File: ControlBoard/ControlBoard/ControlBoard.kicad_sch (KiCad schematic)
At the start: 30 parts, among them J10 PWR_IN, J12 FITPC, J13 SENS, J14 VBAT, J16 5V, J17 FAN, J2 Port, J3 USB_B_Mini, J4 PRT, J5 Stb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

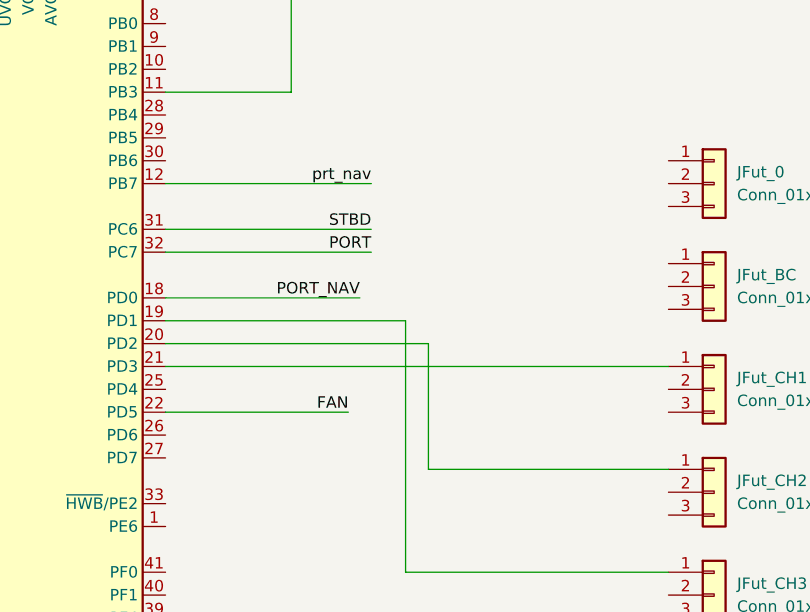
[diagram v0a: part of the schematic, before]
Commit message: Controller board compiling, no real code yet.
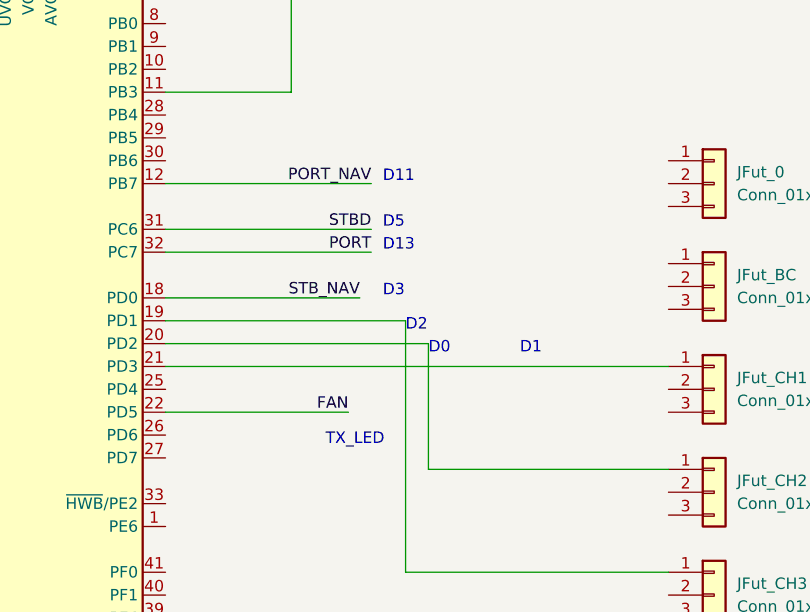
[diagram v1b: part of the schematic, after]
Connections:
- net prt_nav is gone; now on net PORT_NAV: U?.12 (PB7)
- net PORT_NAV: no longer U?.18 (PD0)
- new net STB_NAV: U?.18 (PD0)
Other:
- note added: "D0"
- note added: "D1"
- note added: "D11"
- note added: "D13"
- note added: "D2"
- note added: "D3"
- note added: "D5"
- note added: "TX_LED"
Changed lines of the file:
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@@
     (stroke (width 0) (type default) (color 0 0 0 0))
+  )
+  (text "TX_LED" (at 106.68 99.06 0)
+    (effects (font (size 1.27 1.27)) (justify left bottom))
+  )
+  (text "D1" (at 128.27 88.9 0)
+    (effects (font (size 1.27 1.27)) (justify left bottom))
+  )
+  (text "D11" (at 113.03 69.85 0)
+    (effects (font (size 1.27 1.27)) (justify left bottom))
+  )
+  (text "D5" (at 113.03 74.93 0)
+    (effects (font (size 1.27 1.27)) (justify left bottom))
+  )
+  (text "D13" (at 113.03 77.47 0)
+    (effects (font (size 1.27 1.27)) (justify left bottom))
+  )
+  (text "D3" (at 113.03 82.55 0)
+    (effects (font (size 1.27 1.27)) (justify left bottom))
+  )
+  (text "D2" (at 115.57 86.36 0)
+    (effects (font (size 1.27 1.27)) (justify left bottom))
+  )
+  (text "D0" (at 118.11 88.9 0)
+    (effects (font (size 1.27 1.27)) (justify left bottom))
   )
   (label "MOSI" (at 140.97 44.45 180)
@@
     (effects (font (size 1.27 1.27)) (justify right bottom))
   )
-  (label "PORT_NAV" (at 110.49 82.55 180)
+  (label "STB_NAV" (at 110.49 82.55 180)
     (effects (font (size 1.27 1.27)) (justify right bottom))
   )
@@
     (effects (font (size 1.27 1.27)) (justify left bottom))
   )
-  (label "prt_nav" (at 111.76 69.85 180)
+  (label "PORT_NAV" (at 111.76 69.85 180)
     (effects (font (size 1.27 1.27)) (justify right bottom))
   )

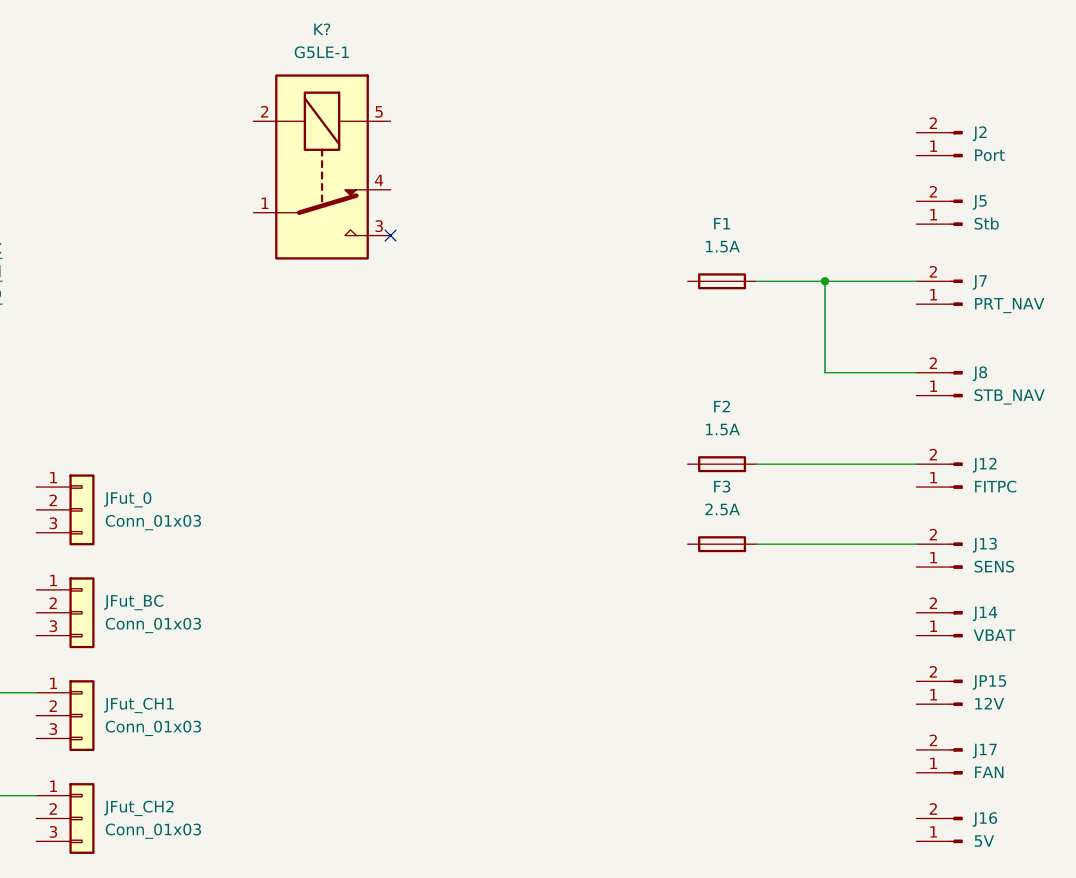
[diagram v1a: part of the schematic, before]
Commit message: added more board details as I discover them and backups and instructions for the existing uC code.
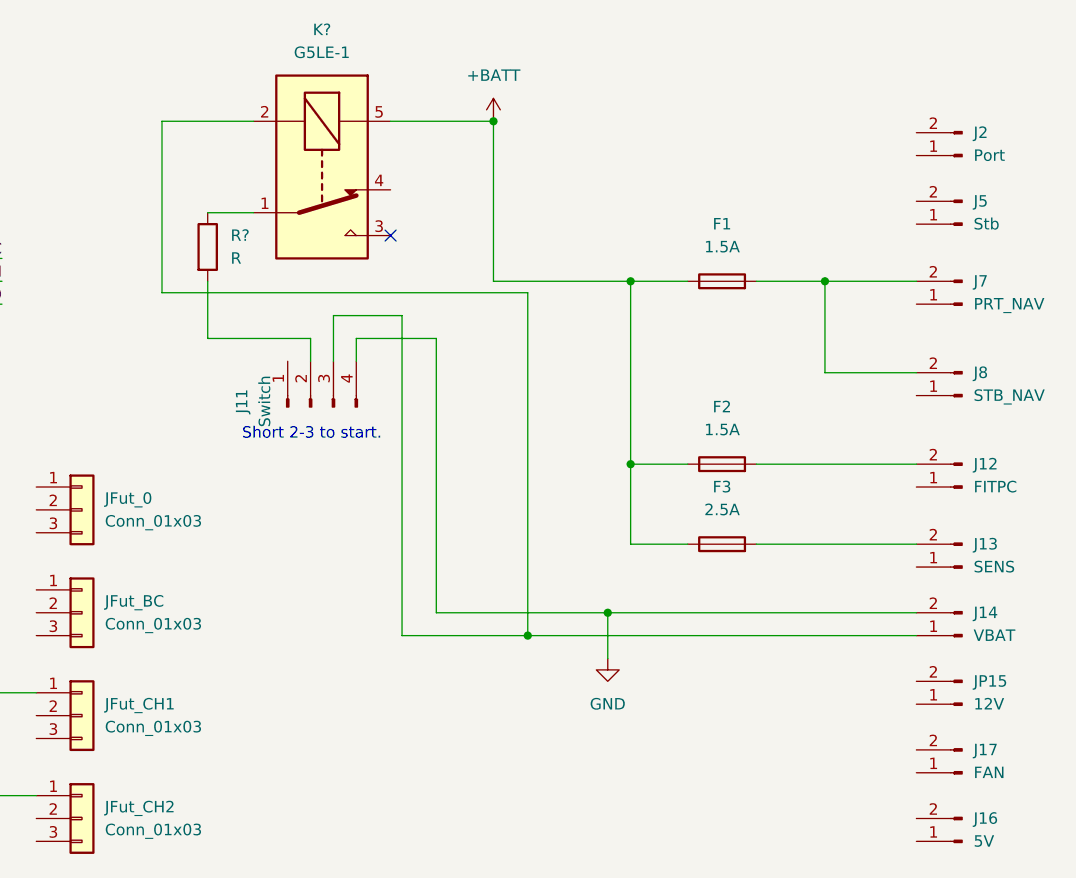
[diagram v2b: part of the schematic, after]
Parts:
- added J11: Switch, symbol Connector:Conn_01x04_Male
- added R?: R, symbol Device:R
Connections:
- net +BATT: now also F1.1, F2.1, F3.1, K?.5
- net GND: now also J14.2 (Pin_2), J11.4 (Pin_4)
- net at K?.1: now also R?.1
- net at K?.2: now also J14.1 (Pin_1), J11.3 (Pin_3)
- new net: J11.2 (Pin_2), R?.2
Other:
- note added: "Short 2-3 to start."

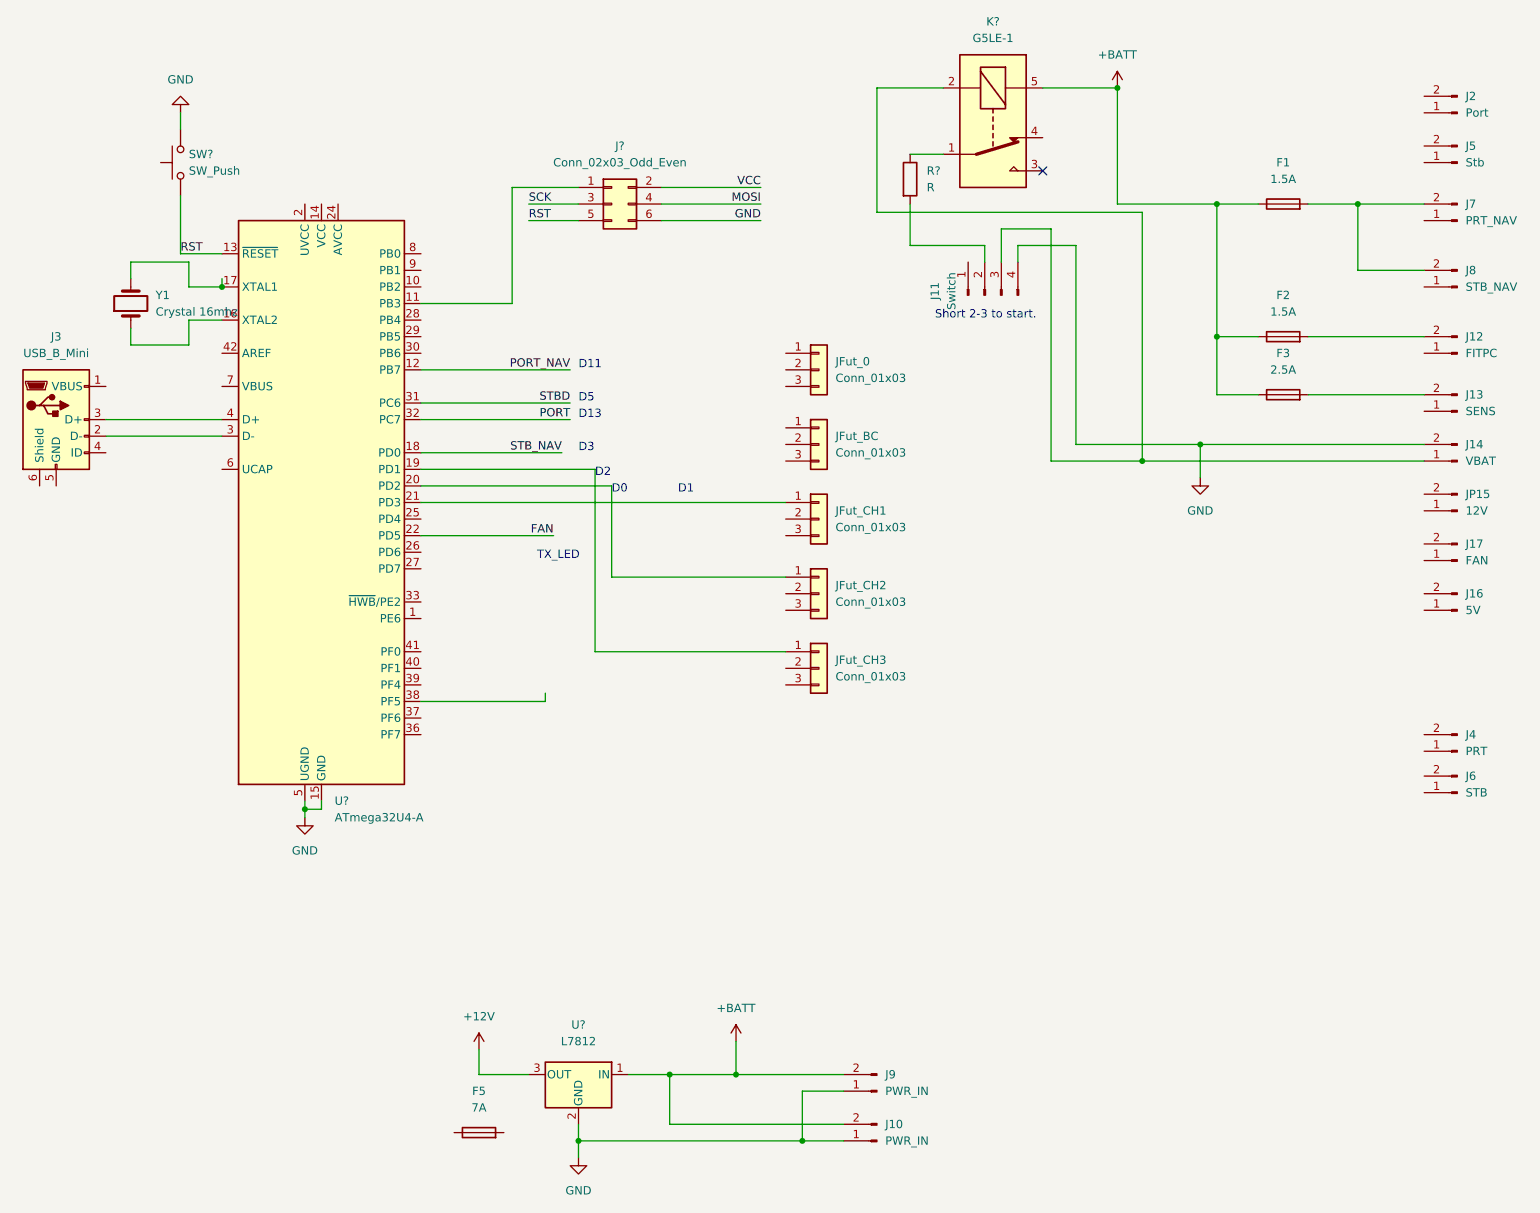
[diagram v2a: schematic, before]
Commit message: updated backup script instructions, updated control board diagram and pinouts.
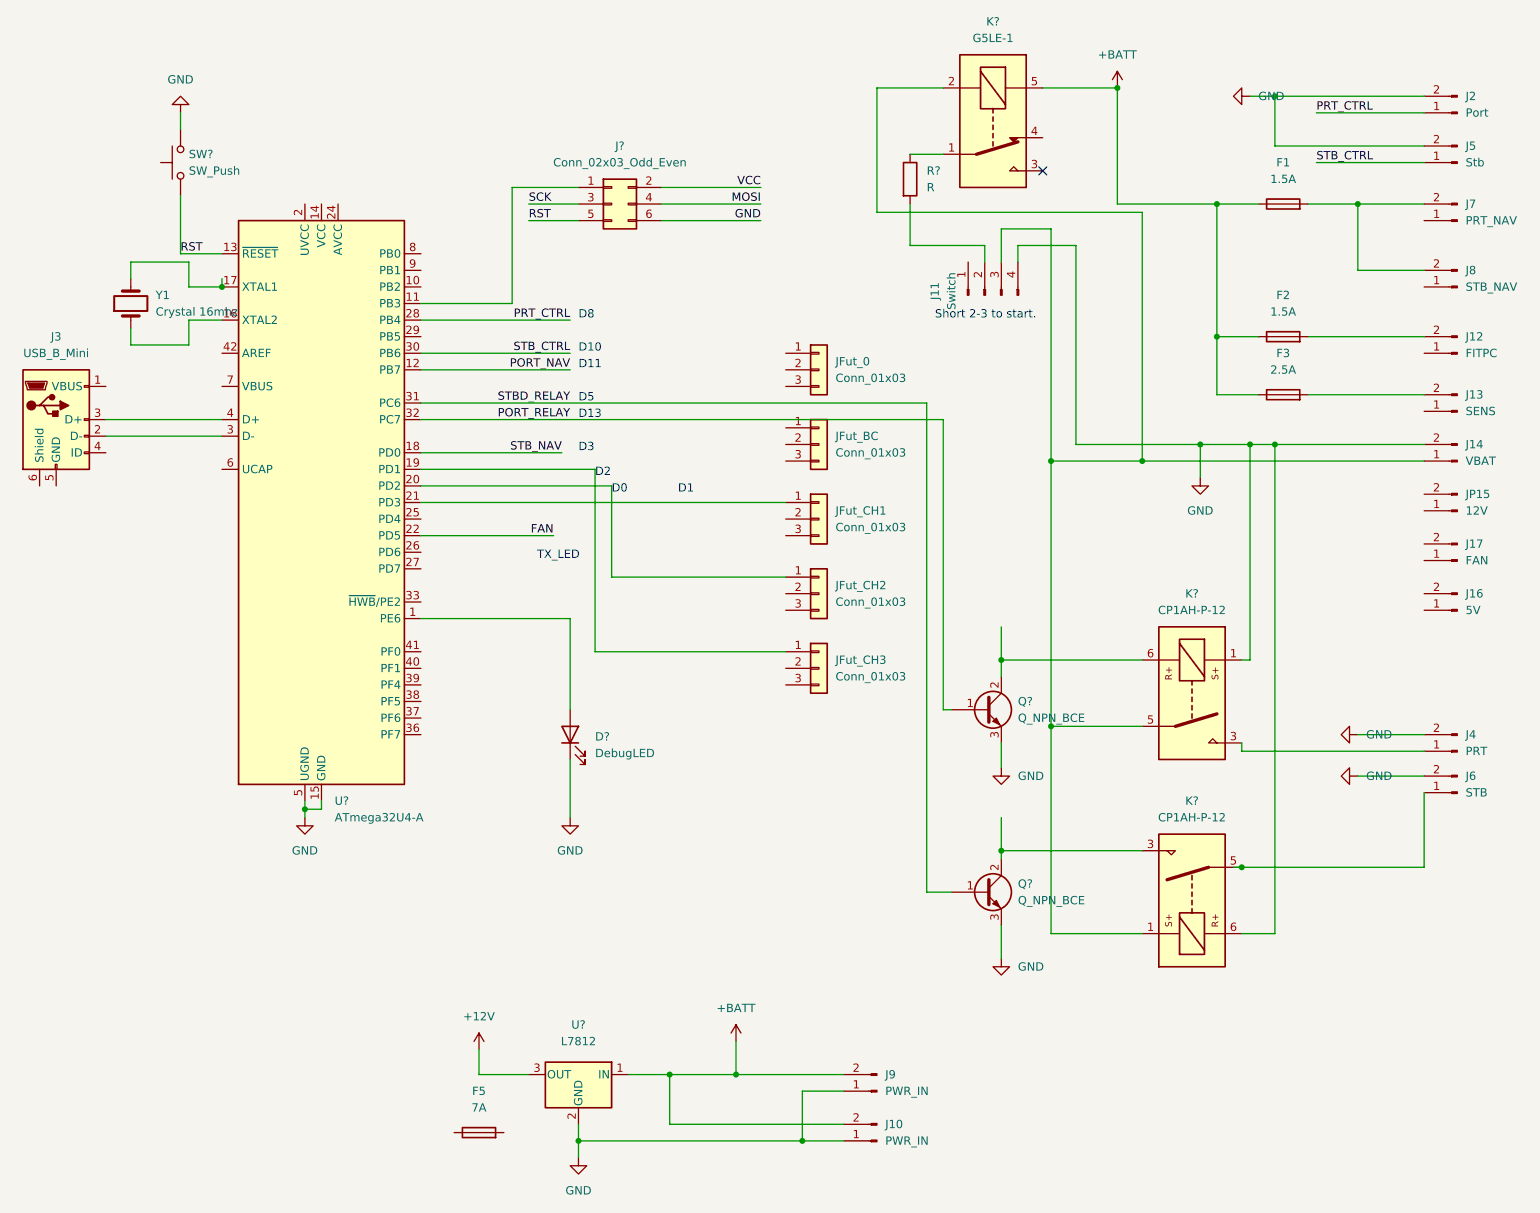
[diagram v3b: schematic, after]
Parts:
- added D?: DebugLED, symbol Device:LED
- added K? (x2): CP1AH-P-12, symbol Relay:ADW11
- added Q? (x2): Q_NPN_BCE, symbol Device:Q_NPN_BCE
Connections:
- net GND: now also J2.2 (Pin_2), J4.2 (Pin_2), J5.2 (Pin_2), J6.2 (Pin_2), D?.1 (K), K?.1, K?.6, Q?.3 (E), Q?.3 (E)
- net at U?.1 (PE6): now also D?.2 (A)
- net PRT_CTRL: now reaches U?.28 (PB4)
- net PRT_CTRL: now also J2.1 (Pin_1)
- net STB_CTRL: now reaches U?.30 (PB6)
- net STB_CTRL: now also J5.1 (Pin_1)
- net at J11.3 (Pin_3), J14.1 (Pin_1), K?.2: now also K?.1, K?.5
- net at J6.1 (Pin_1): now also K?.5
- net at J4.1 (Pin_1): now also K?.3
- net PORT renamed PORT_RELAY
- net PORT_RELAY: now also Q?.1 (B)
- net STBD renamed STBD_RELAY
- net STBD_RELAY: now also Q?.1 (B)
- new net: K?.6, Q?.2 (C)
- new net: K?.3, Q?.2 (C)
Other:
- note added: "D10"
- note added: "D8"

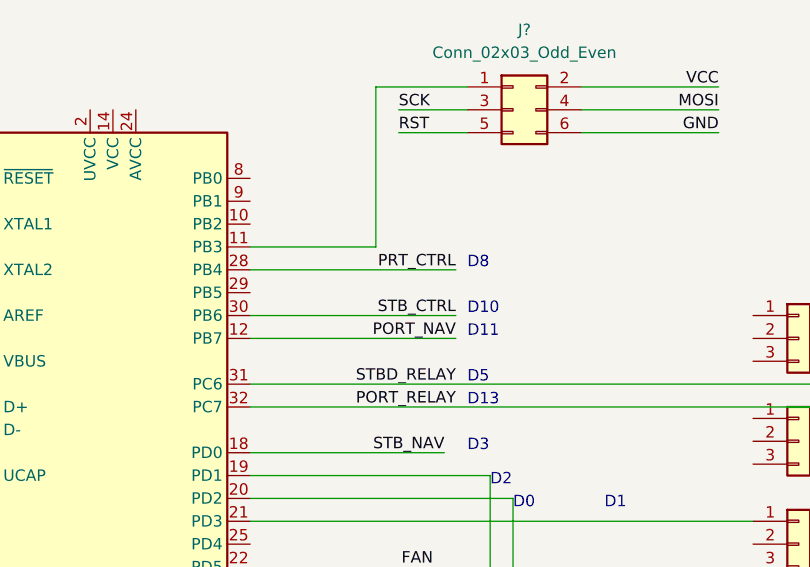
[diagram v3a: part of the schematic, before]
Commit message: Updating code for the uC. Got the types building on the uc too.
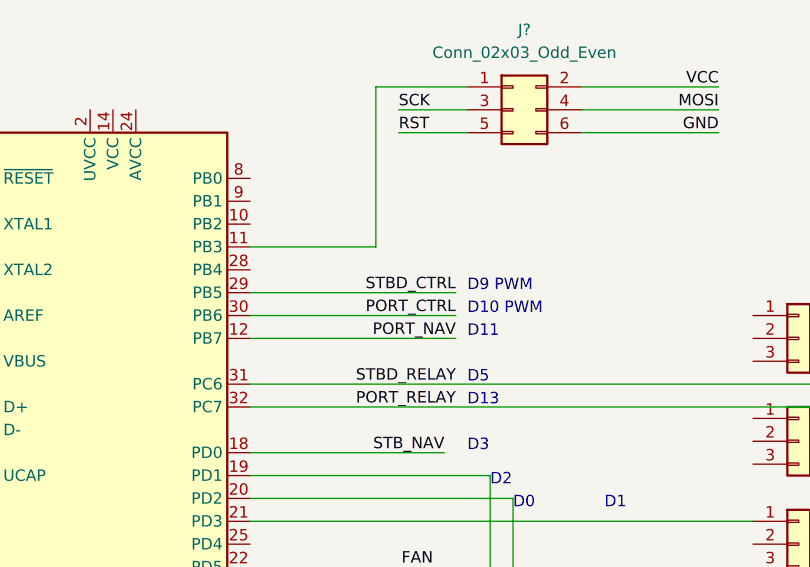
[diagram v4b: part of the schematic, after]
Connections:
- net PRT_CTRL: no longer U?.28 (PB4)
- net STB_CTRL: no longer U?.30 (PB6)
- net STBD_CTRL: now reaches U?.29 (PB5)
- new net PORT_CTRL: U?.30 (PB6)
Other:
- note added: "D10 PWM"
- note added: "D9 PWM"
- note removed: "D10"
- note removed: "D8"
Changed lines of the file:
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@@
-    (stroke (width 0) (type default) (color 0 0 0 0))
-  )
-  (wire (pts (xy 88.9 62.23) (xy 111.76 62.23))
     (stroke (width 0) (type default) (color 0 0 0 0))
   )
@@
     (stroke (width 0) (type default) (color 0 0 0 0))
   )
+  (wire (pts (xy 88.9 64.77) (xy 111.76 64.77))
+    (stroke (width 0) (type default) (color 0 0 0 0))
+  )
   (wire (pts (xy 242.57 83.82) (xy 199.39 83.82))
     (stroke (width 0) (type default) (color 0 0 0 0))
@@
     (stroke (width 0) (type default) (color 0 0 0 0))
   )
-  (text "D10" (at 113.03 67.31 0)
+  (text "D10 PWM" (at 113.03 67.31 0)
     (effects (font (size 1.27 1.27)) (justify left bottom))
   )
@@
     (effects (font (size 1.27 1.27)) (justify left bottom))
   )
-  (text "D8" (at 113.03 62.23 0)
+  (text "D9 PWM" (at 113.03 64.77 0)
     (effects (font (size 1.27 1.27)) (justify left bottom))
   )
@@
     (effects (font (size 1.27 1.27)) (justify left bottom))
   )
+  (label "STBD_CTRL" (at 111.76 64.77 180)
+    (effects (font (size 1.27 1.27)) (justify right bottom))
+  )
   (label "MOSI" (at 140.97 44.45 180)
     (effects (font (size 1.27 1.27)) (justify right bottom))
@@
     (effects (font (size 1.27 1.27)) (justify right bottom))
   )
-  (label "PRT_CTRL" (at 111.76 62.23 180)
-    (effects (font (size 1.27 1.27)) (justify right bottom))
-  )
-  (label "STB_CTRL" (at 111.76 67.31 180)
-    (effects (font (size 1.27 1.27)) (justify right bottom))
-  )
+  (label "PORT_CTRL" (at 111.76 67.31 180)
+    (effects (font (size 1.27 1.27)) (justify right bottom))
+  )
